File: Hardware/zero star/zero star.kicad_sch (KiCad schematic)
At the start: 91 parts, among them J1 USB_C_Receptacle_USB2.0_16P, J10 Conn_01x01, J11 Conn_01x01, J12 Conn_01x01, J13 Conn_01x01, J14 Conn_01x01, J15 Conn_01x01, J16 Conn_01x01, J17 Conn_01x01, J18 Conn_01x01, J19 Conn_01x01, J2 Conn_01x01, J20 Conn_01x01, J21 Conn_01x01, J22 ELRS, J23 GPS, J24 Conn_01x01, J25 Conn_01x01, J26 Conn_01x01, J27 Conn_01x01, J28 Conn_01x01, J29 Conn_01x01, J299 Conn_01x01, J3 上位机, J30 Conn_01x01, J31 Conn_01x01, J32 Conn_01x01, J33 Conn_01x01, J4 4-in-1 ESC, J5 光流, J6 VTX, J7 Conn_01x01, J8 Conn_01x01, J9 Conn_01x01, SW1 SW_SPST, U1 STM32F405RGTx, U10 RT9193-33, U2 SY8303AIC, U3 SY8303AIC, U4 RT9193-33, Y1 8Mhz

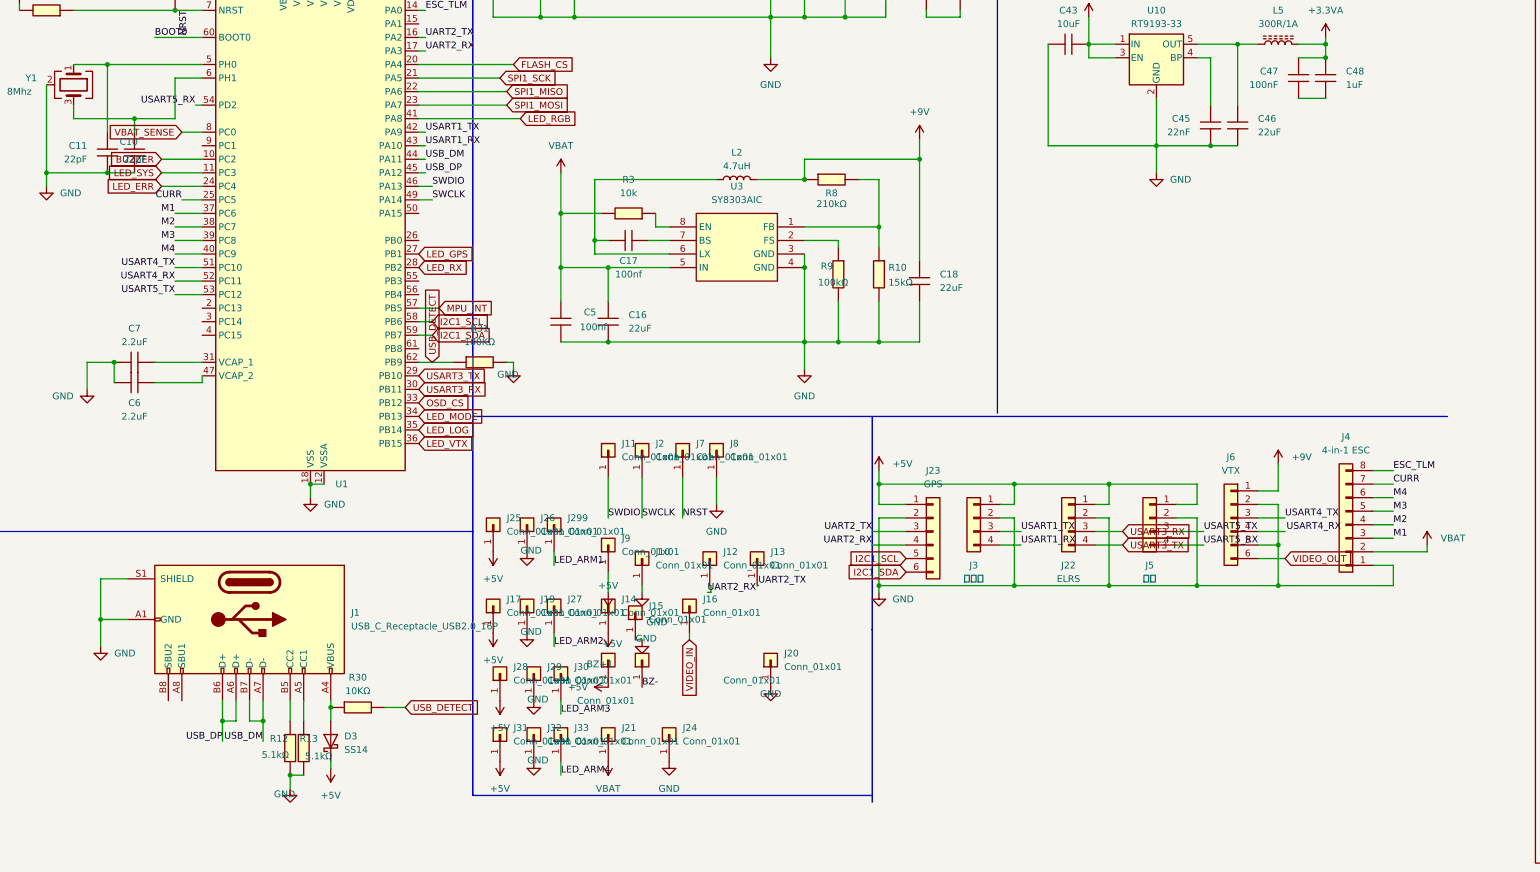
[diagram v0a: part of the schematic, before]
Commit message: HW v2.5.7: SPI CS pin swap, PCB layout v1, CubeMX update
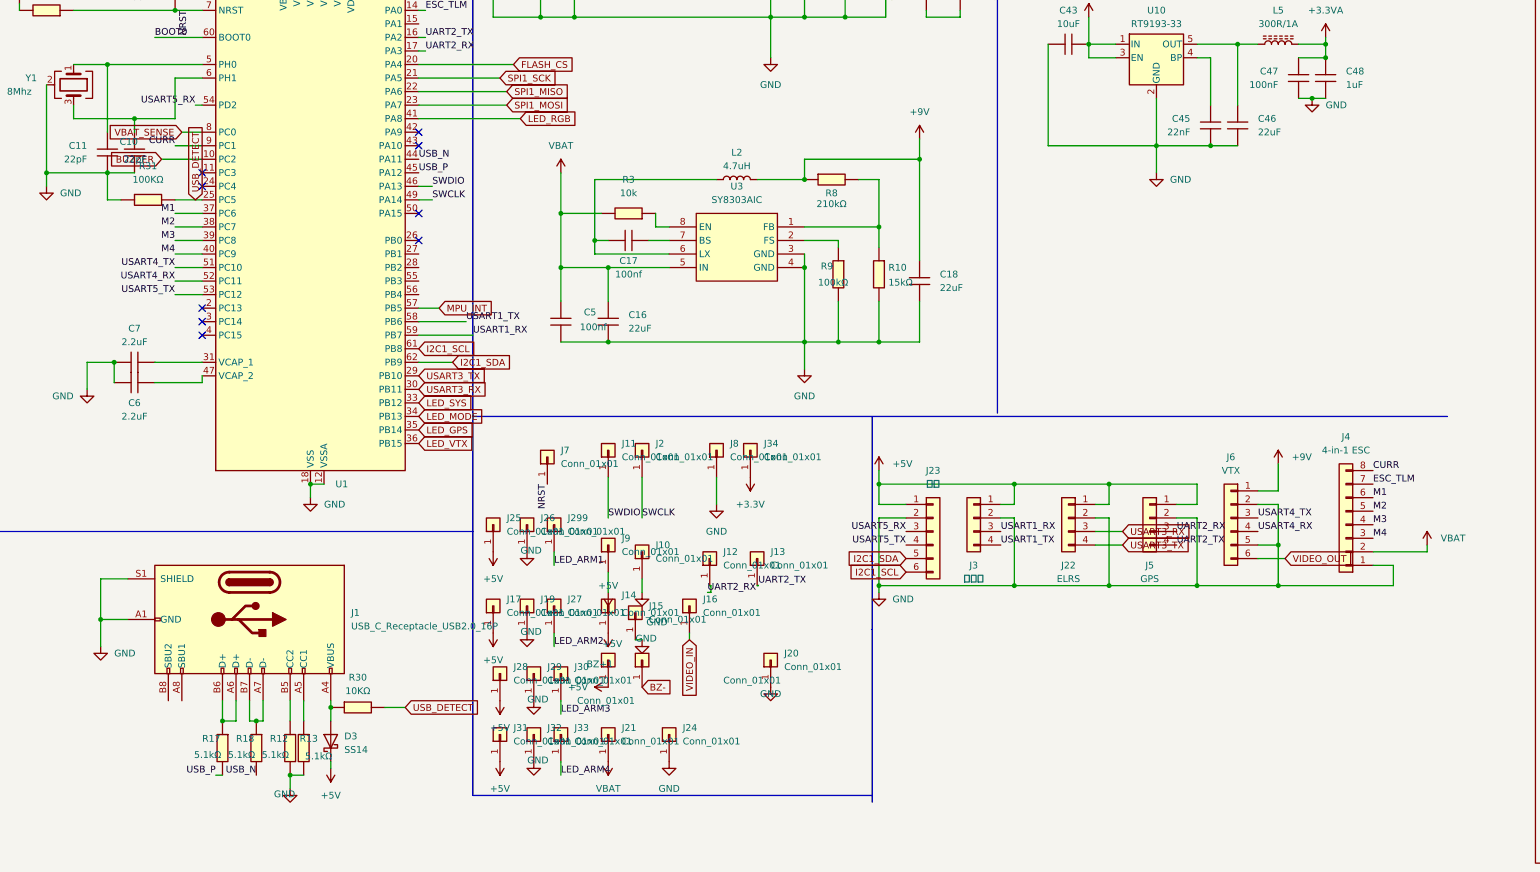
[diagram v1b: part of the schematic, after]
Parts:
- added J34: Conn_01x01, Connector_Wire:SolderWirePad_1x01_SMD_1x2mm, symbol Connector_Generic:Conn_01x01
- added R17, R18: 5.1kΩ, PCM_fab:R_0603, symbol PCM_fab:R_0603
- BZ+1, J10, J11, J12, J13, J14, J15, J16, J17, J18, J19, J2, J20, J21, J24, J25, J26, J27, J28, J29, J299, J30, J31, J32, J33, J7, J8, J9: footprint TestPoint:TestPoint_Pad_2.0x2.0mm -> Connector_Wire:SolderWirePad_1x01_SMD_1x2mm
- J23: value GPS -> 光流
- J5: value 光流 -> GPS
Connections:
- net LED_LOG is gone; now on net LED_GPS: U1.35 (PB14)
- net OSD_CS is gone; now on net LED_SYS: U1.33 (PB12)
- net +3.3V: now also J34.1 (Pin_1)
- net CURR: now also J4.8 (Pin_8), U1.9 (PC1); no longer J4.7 (Pin_7), U1.25 (PC5)
- net ESC_TLM: now also J4.7 (Pin_7); no longer J4.8 (Pin_8)
- net GND: now also C47.2, C48.2, R31.2; no longer R31.1
- net I2C1_SCL: now also J23.6 (Pin_6), U1.61 (PB8); no longer J23.5 (Pin_5), U1.58 (PB6)
- net I2C1_SDA: now also J23.5 (Pin_5), U1.62 (PB9); no longer J23.6 (Pin_6), U1.59 (PB7)
- net LED_GPS: no longer U1.27 (PB1)
- net LED_SYS: no longer U1.11 (PC3)
- net M1: now also J4.6 (Pin_6); no longer J4.3 (Pin_3)
- net M2: now also J4.5 (Pin_5); no longer J4.4 (Pin_4)
- net M3: now also J4.4 (Pin_4); no longer J4.5 (Pin_5)
- net M4: now also J4.3 (Pin_3); no longer J4.6 (Pin_6)
- net UART2_RX: now also J5.3 (Pin_3); no longer J23.4 (Pin_4)
- net UART2_TX: now also J5.4 (Pin_4); no longer J23.3 (Pin_3)
- net USART1_RX: now also J3.3 (Pin_3), U1.59 (PB7); no longer J3.4 (Pin_4), U1.43 (PA10)
- net USART1_TX: now also J3.4 (Pin_4), U1.58 (PB6); no longer J3.3 (Pin_3), U1.42 (PA9)
- net USART4_RX: now also J6.4 (Pin_4)
- net USART5_RX: now also J23.3 (Pin_3); no longer J5.4 (Pin_4)
- net USART5_TX: now also J23.4 (Pin_4); no longer J5.3 (Pin_3)
- net USB_DETECT: now also R31.1, U1.25 (PC5); no longer R31.2, U1.62 (PB9)
- net LED_ERR: no longer names the net of U1.24 (PC4)
- net LED_RX: no longer names the net of U1.28 (PB2)
- net USB_DM: no longer names the net of J1.A7 (D-), J1.B7 (D-)
- net USB_DM: now also R18.2; no longer U1.44 (PA11)
- net USB_DP: no longer names the net of J1.A6 (D+), J1.B6 (D+)
- net USB_DP: now also R17.2; no longer U1.45 (PA12)
- new net USB_N: R18.1, U1.44 (PA11)
- new net USB_P: R17.1, U1.45 (PA12)
- no-connect marks 0 -> 9
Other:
- moved on the sheet: J10, R31
